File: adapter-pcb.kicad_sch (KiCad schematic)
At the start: 0 parts

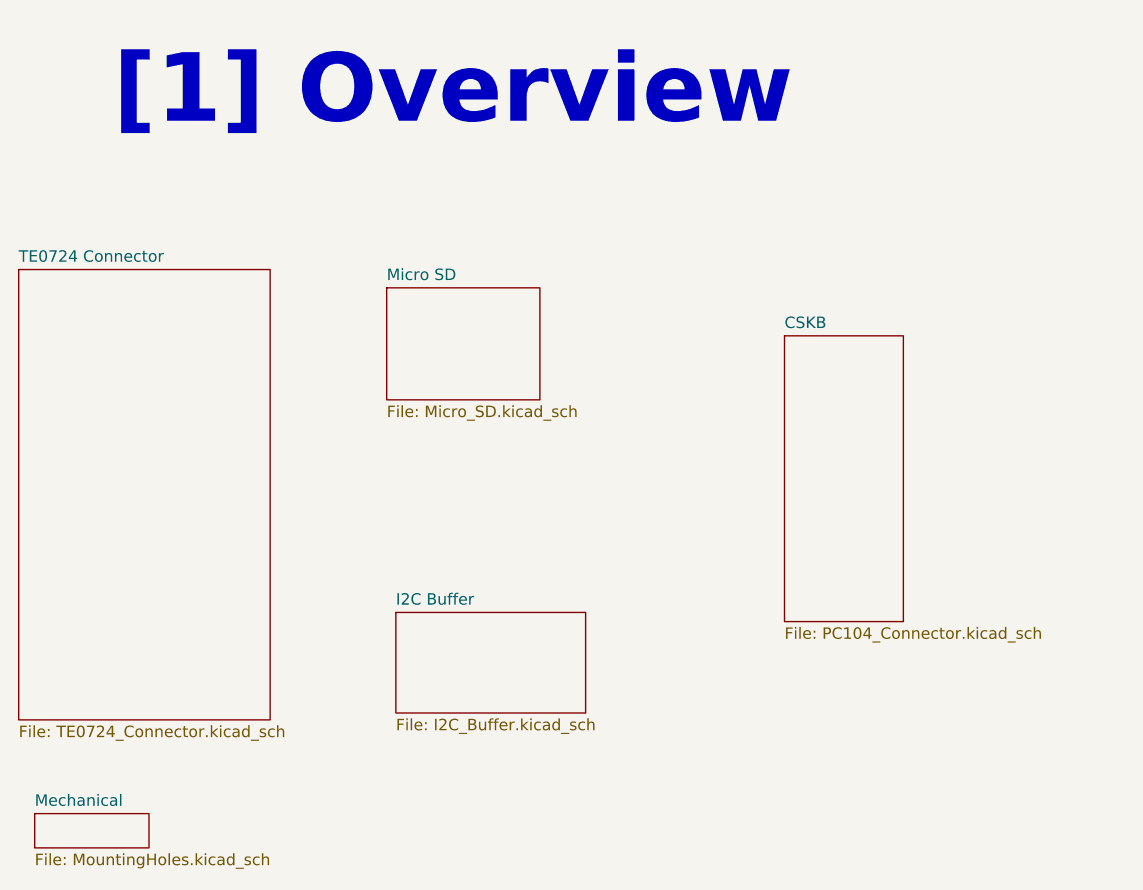
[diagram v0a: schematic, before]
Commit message: Added hierarchical lables to the schematic
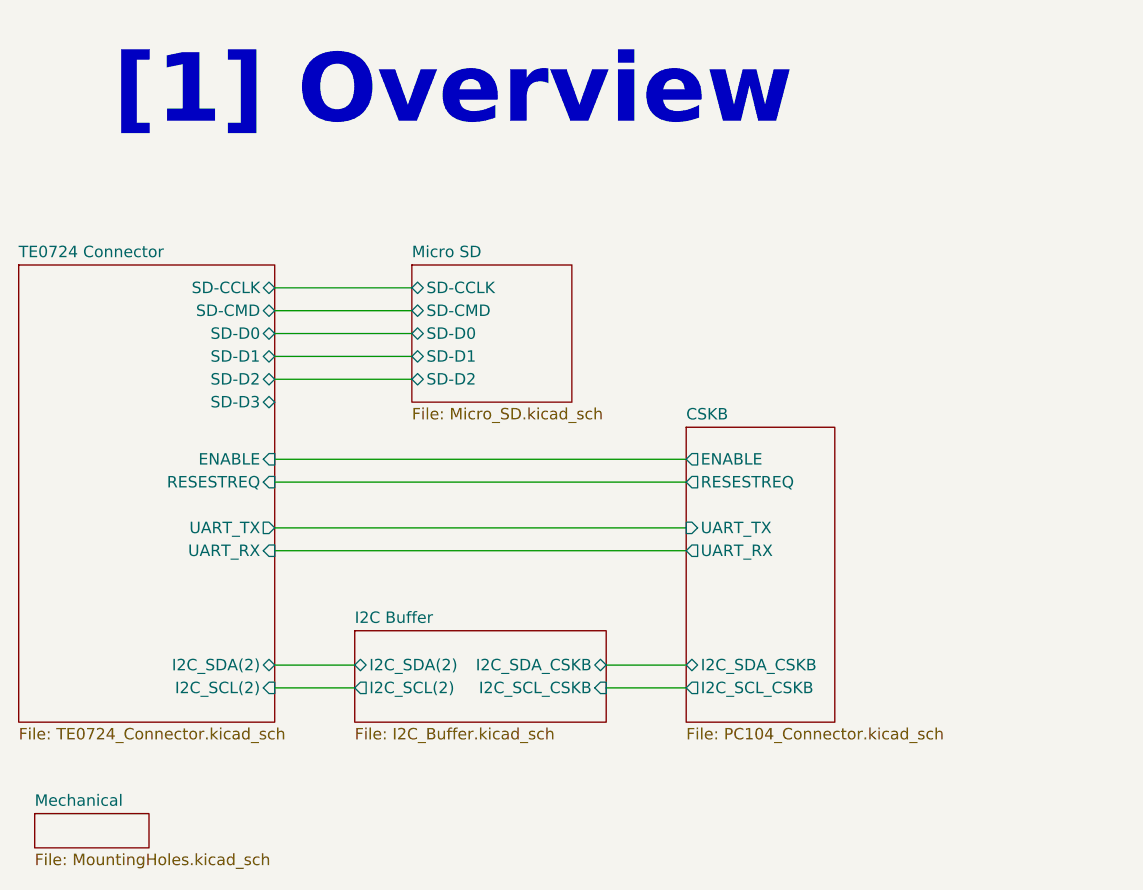
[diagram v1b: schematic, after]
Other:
- sheet CSKB ports: added ENABLE, I2C_SCL_CSKB, I2C_SDA_CSKB, RESESTREQ, UART_RX, UART_TX; removed none
- sheet I2C Buffer ports: added I2C_SCL(2), I2C_SCL_CSKB, I2C_SDA(2), I2C_SDA_CSKB; removed none
- sheet Micro SD ports: added SD-CCLK, SD-CMD, SD-D0, SD-D1, SD-D2; removed none
- sheet TE0724 Connector ports: added ENABLE, I2C_SCL(2), I2C_SDA(2), RESESTREQ, SD-CCLK, SD-CMD, SD-D0, SD-D1, SD-D2, SD-D3, UART_RX, UART_TX; removed none
